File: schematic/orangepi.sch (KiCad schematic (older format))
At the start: 2 parts, among them J18 Conn_02x13_Odd_Even

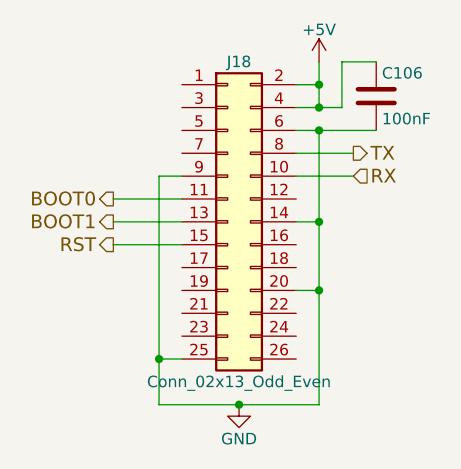
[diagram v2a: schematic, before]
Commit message: Routed signals to pi connector
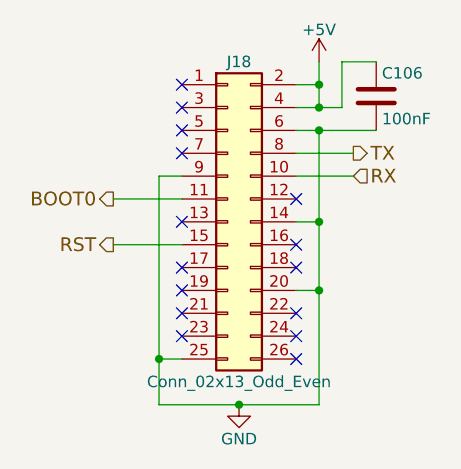
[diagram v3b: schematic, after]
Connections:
- net BOOT1: no longer names the net of J18.13 (Pin_13)
- no-connect marks 0 -> 15
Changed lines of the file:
@@
 Text HLabel 5200 3600 0    60   Output ~ 0
 BOOT0
-Text HLabel 5200 3700 0    60   Output ~ 0
-BOOT1
-Wire Wire Line
-	5500 3700 5200 3700
 Wire Wire Line
 	5500 3600 5200 3600
@@
 Wire Wire Line
 	5500 3800 5200 3800
+NoConn ~ 5500 3100
+NoConn ~ 5500 3200
+NoConn ~ 5500 3300
+NoConn ~ 5500 3400
+NoConn ~ 5500 3700
+NoConn ~ 5500 3900
+NoConn ~ 5500 4000
+NoConn ~ 5500 4100
+NoConn ~ 5500 4200
+NoConn ~ 6000 3600
+NoConn ~ 6000 3800
+NoConn ~ 6000 3900
+NoConn ~ 6000 4100
+NoConn ~ 6000 4200
+NoConn ~ 6000 4300
 $EndSCHEMATC

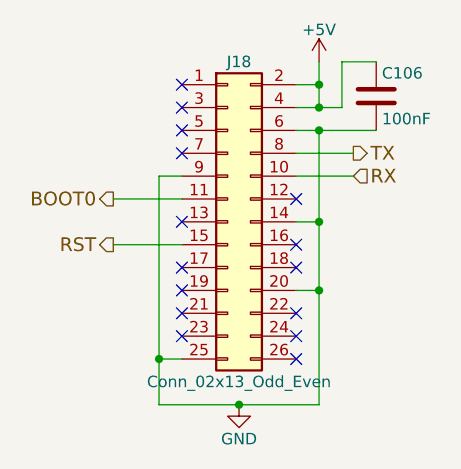
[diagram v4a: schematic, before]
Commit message: Switch orange pi to raspberry pi zero w because the price difference is small
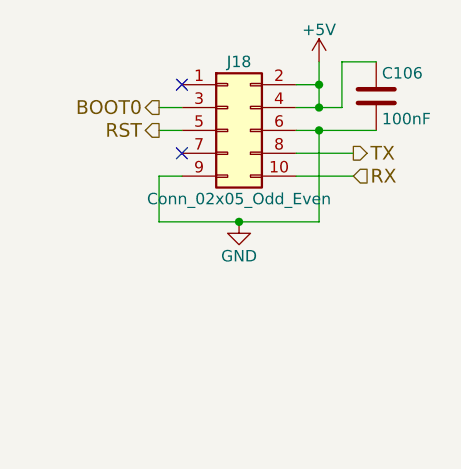
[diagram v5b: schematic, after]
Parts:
- removed J18: Conn_02x13_Odd_Even, Socket_Strips:Socket_Strip_Straight_2x13_Pitch2.54mm, symbol Conn_02x13_Odd_Even
- added J18: Conn_02x05_Odd_Even, Pin_Headers:Pin_Header_Straight_2x05_Pitch2.54mm, symbol Conn_02x05_Odd_Even
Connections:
- net +5V: now also J18.2 (Pin_2), J18.4 (Pin_4)
- net BOOT0: now also J18.3 (Pin_3)
- net GND: now also J18.6 (Pin_6), J18.9 (Pin_9)
- net RST: now also J18.5 (Pin_5)
- net RX: now also J18.10 (Pin_10)
- net TX: now also J18.8 (Pin_8)
- no-connect marks 15 -> 2
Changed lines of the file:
@@
 $EndDescr
 $Comp
-L Conn_02x13_Odd_Even J18
-U 1 1 59F4D38E
-P 5700 3700
-F 0 "J18" H 5750 4400 50  0000 C CNN
-F 1 "Conn_02x13_Odd_Even" H 5750 3000 50  0000 C CNN
-F 2 "Socket_Strips:Socket_Strip_Straight_2x13_Pitch2.54mm" H 5700 3700 50  0001 C CNN
-F 3 "" H 5700 3700 50  0001 C CNN
-	1    5700 3700
-	1    0    0    -1
-$EndComp
-$Comp
-L +5V #PWR0156
+L +5V #PWR157
 U 1 1 59F4D3CF
 P 6100 3000
-F 0 "#PWR0156" H 6100 2850 50  0001 C CNN
+F 0 "#PWR157" H 6100 2850 50  0001 C CNN
 F 1 "+5V" H 6100 3140 50  0000 C CNN
 F 2 "" H 6100 3000 50  0001 C CNN
@@
 	6000 3300 6350 3300
 Wire Wire Line
-	6100 4500 6100 3300
-Wire Wire Line
-	6000 3700 6100 3700
-Connection ~ 6100 3700
-Wire Wire Line
-	6000 4000 6100 4000
-Connection ~ 6100 4000
-Wire Wire Line
 	5500 3500 5400 3500
-Wire Wire Line
-	5400 3500 5400 4500
-Wire Wire Line
-	5400 4500 6100 4500
-Wire Wire Line
-	5400 4300 5500 4300
-Connection ~ 5400 4300
 $Comp
-L GND #PWR0157
+L GND #PWR156
 U 1 1 59F4D42B
-P 5750 4500
-F 0 "#PWR0157" H 5750 4250 50  0001 C CNN
-F 1 "GND" H 5750 4350 50  0000 C CNN
-F 2 "" H 5750 4500 50  0001 C CNN
-F 3 "" H 5750 4500 50  0001 C CNN
-	1    5750 4500
+P 5750 3700
+F 0 "#PWR156" H 5750 3450 50  0001 C CNN
+F 1 "GND" H 5750 3550 50  0000 C CNN
+F 2 "" H 5750 3700 50  0001 C CNN
+F 3 "" H 5750 3700 50  0001 C CNN
+	1    5750 3700
 	1    0    0    -1
 $EndComp
-Connection ~ 5750 4500
 Text HLabel 6250 3400 2    60   Output ~ 0
 TX
@@
 	6200 3000 6350 3000
 Connection ~ 6100 3200
-Text HLabel 5200 3600 0    60   Output ~ 0
+Text HLabel 5400 3200 0    60   Output ~ 0
 BOOT0
 Wire Wire Line
-	5500 3600 5200 3600
-Text HLabel 5200 3800 0    60   Output ~ 0
+	5500 3200 5400 3200
+Text HLabel 5400 3300 0    60   Output ~ 0
 RST
 Wire Wire Line
-	5500 3800 5200 3800
+	5500 3300 5400 3300
 NoConn ~ 5500 3100
-NoConn ~ 5500 3200
-NoConn ~ 5500 3300
 NoConn ~ 5500 3400
-NoConn ~ 5500 3700
-NoConn ~ 5500 3900
-NoConn ~ 5500 4000
-NoConn ~ 5500 4100
-NoConn ~ 5500 4200
-NoConn ~ 6000 3600
-NoConn ~ 6000 3800
-NoConn ~ 6000 3900
-NoConn ~ 6000 4100
-NoConn ~ 6000 4200
-NoConn ~ 6000 4300
+$Comp
+L Conn_02x05_Odd_Even J18
+U 1 1 5A77AA6E
+P 5700 3300
+F 0 "J18" H 5750 3600 50  0000 C CNN
+F 1 "Conn_02x05_Odd_Even" H 5750 3000 50  0000 C CNN
+F 2 "Pin_Headers:Pin_Header_Straight_2x05_Pitch2.54mm" H 5700 3300 50  0001 C CNN
+F 3 "" H 5700 3300 50  0001 C CNN
+	1    5700 3300
+	1    0    0    -1
+$EndComp
+Wire Wire Line
+	5400 3500 5400 3700
+Wire Wire Line
+	6100 3300 6100 3700
+Wire Wire Line
+	6100 3700 5400 3700
+Connection ~ 5750 3700
 $EndSCHEMATC

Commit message: Updated to kicad 5.0.0
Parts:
- C106: symbol C -> Device:C
- J18: symbol Conn_02x05_Odd_Even -> Connector_Generic:Conn_02x05_Odd_Even
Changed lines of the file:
@@
-EESchema Schematic File Version 2
-LIBS:74xgxx
-LIBS:74xx
-LIBS:ac-dc
-LIBS:actel
-LIBS:adc-dac
-LIBS:allegro
-LIBS:Altera
-LIBS:analog_devices
-LIBS:analog_switches
-LIBS:atmel
-LIBS:audio
-LIBS:battery_management
-LIBS:bbd
-LIBS:bosch
-LIBS:brooktre
-LIBS:cmos4000
-LIBS:cmos_ieee
-LIBS:conn
-LIBS:contrib
-LIBS:cypress
-LIBS:dc-dc
-LIBS:device
-LIBS:digital-audio
-LIBS:diode
-LIBS:display
-LIBS:dsp
-LIBS:elec-unifil
-LIBS:ESD_Protection
-LIBS:ftdi
-LIBS:gennum
-LIBS:graphic_symbols
-LIBS:hc11
-LIBS:infineon
-LIBS:intel
-LIBS:interface
-LIBS:intersil
-LIBS:ir
-LIBS:Lattice
-LIBS:leds
-LIBS:LEM
-LIBS:linear
-LIBS:logic_programmable
-LIBS:maxim
-LIBS:mechanical
-LIBS:memory
-LIBS:microchip
-LIBS:microchip_dspic33dsc
-LIBS:microchip_pic10mcu
-LIBS:microchip_pic12mcu
-LIBS:microchip_pic16mcu
-LIBS:microchip_pic18mcu
-LIBS:microchip_pic24mcu
-LIBS:microchip_pic32mcu
-LIBS:microcontrollers
-LIBS:modules
-LIBS:motor_drivers
-LIBS:motorola
-LIBS:motors
-LIBS:msp430
-LIBS:nordicsemi
-LIBS:nxp
-LIBS:nxp_armmcu
-LIBS:onsemi
-LIBS:opto
-LIBS:Oscillators
-LIBS:philips
-LIBS:power
-LIBS:powerint
-LIBS:Power_Management
-LIBS:pspice
-LIBS:references
-LIBS:regul
-LIBS:relays
-LIBS:rfcom
-LIBS:RFSolutions
-LIBS:sensors
-LIBS:silabs
-LIBS:siliconi
-LIBS:stm8
-LIBS:stm32
-LIBS:supertex
-LIBS:switches
-LIBS:texas
-LIBS:transf
-LIBS:transistors
-LIBS:triac_thyristor
-LIBS:ttl_ieee
-LIBS:valves
-LIBS:video
-LIBS:wiznet
-LIBS:Worldsemi
-LIBS:Xicor
-LIBS:xilinx
-LIBS:zetex
-LIBS:Zilog
-LIBS:bd9e302efj
-LIBS:psmn1
-LIBS:tmc2130
+EESchema Schematic File Version 4
 LIBS:schematic-cache
-EELAYER 25 0
+EELAYER 26 0
 EELAYER END
 $Descr A4 11693 8268
@@
 $EndDescr
 $Comp
-L +5V #PWR157
+L power:+5V #PWR0157
 U 1 1 59F4D3CF
 P 6100 3000
-F 0 "#PWR157" H 6100 2850 50  0001 C CNN
+F 0 "#PWR0157" H 6100 2850 50  0001 C CNN
 F 1 "+5V" H 6100 3140 50  0000 C CNN
 F 2 "" H 6100 3000 50  0001 C CNN
@@
 	5500 3500 5400 3500
 $Comp
-L GND #PWR156
+L power:GND #PWR0156
 U 1 1 59F4D42B
 P 5750 3700
-F 0 "#PWR156" H 5750 3450 50  0001 C CNN
+F 0 "#PWR0156" H 5750 3450 50  0001 C CNN
 F 1 "GND" H 5750 3550 50  0000 C CNN
 F 2 "" H 5750 3700 50  0001 C CNN
@@
 	6000 3500 6250 3500
 $Comp
-L C C106
+L Device:C C106
 U 1 1 59F4D4BA
 P 6350 3150
+AR Path="/59F4D4BA" Ref="C106"  Part="1"
+AR Path="/59F4D27D/59F4D4BA" Ref="C106"  Part="1"
 F 0 "C106" H 6375 3250 50  0000 L CNN
 F 1 "100nF" H 6375 3050 50  0000 L CNN
@@
 NoConn ~ 5500 3400
 $Comp
-L Conn_02x05_Odd_Even J18
+L Connector_Generic:Conn_02x05_Odd_Even J18
 U 1 1 5A77AA6E
 P 5700 3300

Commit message: Revert "Updated to kicad 5.0.0"
This reverts commit 6c14fa6c8e6361c9b9ee4065803a5a63755fc6a7.
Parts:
- C106: symbol Device:C -> C
- J18: symbol Connector_Generic:Conn_02x05_Odd_Even -> Conn_02x05_Odd_Even
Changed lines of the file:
@@
-EESchema Schematic File Version 4
+EESchema Schematic File Version 2
+LIBS:74xgxx
+LIBS:74xx
+LIBS:ac-dc
+LIBS:actel
+LIBS:adc-dac
+LIBS:allegro
+LIBS:Altera
+LIBS:analog_devices
+LIBS:analog_switches
+LIBS:atmel
+LIBS:audio
+LIBS:battery_management
+LIBS:bbd
+LIBS:bosch
+LIBS:brooktre
+LIBS:cmos4000
+LIBS:cmos_ieee
+LIBS:conn
+LIBS:contrib
+LIBS:cypress
+LIBS:dc-dc
+LIBS:device
+LIBS:digital-audio
+LIBS:diode
+LIBS:display
+LIBS:dsp
+LIBS:elec-unifil
+LIBS:ESD_Protection
+LIBS:ftdi
+LIBS:gennum
+LIBS:graphic_symbols
+LIBS:hc11
+LIBS:infineon
+LIBS:intel
+LIBS:interface
+LIBS:intersil
+LIBS:ir
+LIBS:Lattice
+LIBS:leds
+LIBS:LEM
+LIBS:linear
+LIBS:logic_programmable
+LIBS:maxim
+LIBS:mechanical
+LIBS:memory
+LIBS:microchip
+LIBS:microchip_dspic33dsc
+LIBS:microchip_pic10mcu
+LIBS:microchip_pic12mcu
+LIBS:microchip_pic16mcu
+LIBS:microchip_pic18mcu
+LIBS:microchip_pic24mcu
+LIBS:microchip_pic32mcu
+LIBS:microcontrollers
+LIBS:modules
+LIBS:motor_drivers
+LIBS:motorola
+LIBS:motors
+LIBS:msp430
+LIBS:nordicsemi
+LIBS:nxp
+LIBS:nxp_armmcu
+LIBS:onsemi
+LIBS:opto
+LIBS:Oscillators
+LIBS:philips
+LIBS:power
+LIBS:powerint
+LIBS:Power_Management
+LIBS:pspice
+LIBS:references
+LIBS:regul
+LIBS:relays
+LIBS:rfcom
+LIBS:RFSolutions
+LIBS:sensors
+LIBS:silabs
+LIBS:siliconi
+LIBS:stm8
+LIBS:stm32
+LIBS:supertex
+LIBS:switches
+LIBS:texas
+LIBS:transf
+LIBS:transistors
+LIBS:triac_thyristor
+LIBS:ttl_ieee
+LIBS:valves
+LIBS:video
+LIBS:wiznet
+LIBS:Worldsemi
+LIBS:Xicor
+LIBS:xilinx
+LIBS:zetex
+LIBS:Zilog
+LIBS:bd9e302efj
+LIBS:psmn1
+LIBS:tmc2130
 LIBS:schematic-cache
-EELAYER 26 0
+EELAYER 25 0
 EELAYER END
 $Descr A4 11693 8268
@@
 $EndDescr
 $Comp
-L power:+5V #PWR0157
+L +5V #PWR157
 U 1 1 59F4D3CF
 P 6100 3000
-F 0 "#PWR0157" H 6100 2850 50  0001 C CNN
+F 0 "#PWR157" H 6100 2850 50  0001 C CNN
 F 1 "+5V" H 6100 3140 50  0000 C CNN
 F 2 "" H 6100 3000 50  0001 C CNN
@@
 	5500 3500 5400 3500
 $Comp
-L power:GND #PWR0156
+L GND #PWR156
 U 1 1 59F4D42B
 P 5750 3700
-F 0 "#PWR0156" H 5750 3450 50  0001 C CNN
+F 0 "#PWR156" H 5750 3450 50  0001 C CNN
 F 1 "GND" H 5750 3550 50  0000 C CNN
 F 2 "" H 5750 3700 50  0001 C CNN
@@
 	6000 3500 6250 3500
 $Comp
-L Device:C C106
+L C C106
 U 1 1 59F4D4BA
 P 6350 3150
-AR Path="/59F4D4BA" Ref="C106"  Part="1"
-AR Path="/59F4D27D/59F4D4BA" Ref="C106"  Part="1"
 F 0 "C106" H 6375 3250 50  0000 L CNN
 F 1 "100nF" H 6375 3050 50  0000 L CNN
@@
 NoConn ~ 5500 3400
 $Comp
-L Connector_Generic:Conn_02x05_Odd_Even J18
+L Conn_02x05_Odd_Even J18
 U 1 1 5A77AA6E
 P 5700 3300
